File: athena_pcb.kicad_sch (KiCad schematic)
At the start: 36 parts, among them J2 Conn_01x04, SW1 SW_Push, U1 NRF5340-QKAA-R7, U2 BME280, Y1 32MHz, Y2 32.768kHz

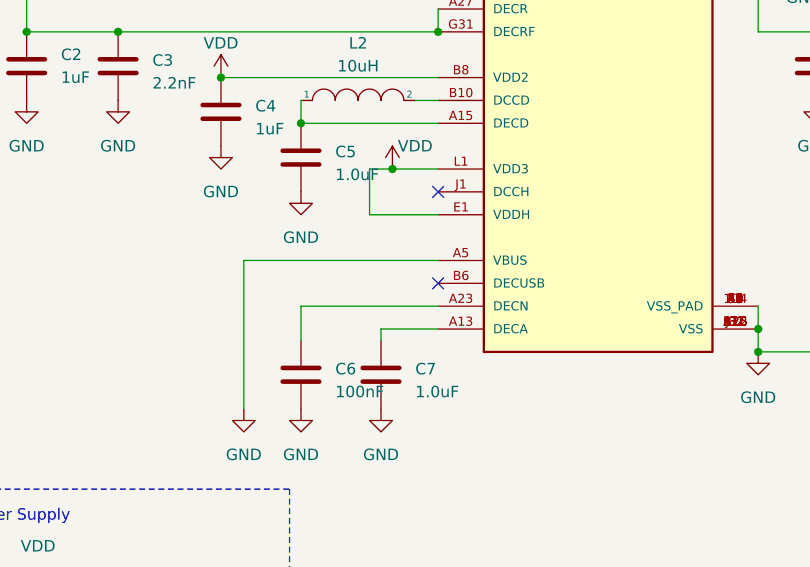
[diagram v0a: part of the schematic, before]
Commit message: Added items in the BOM
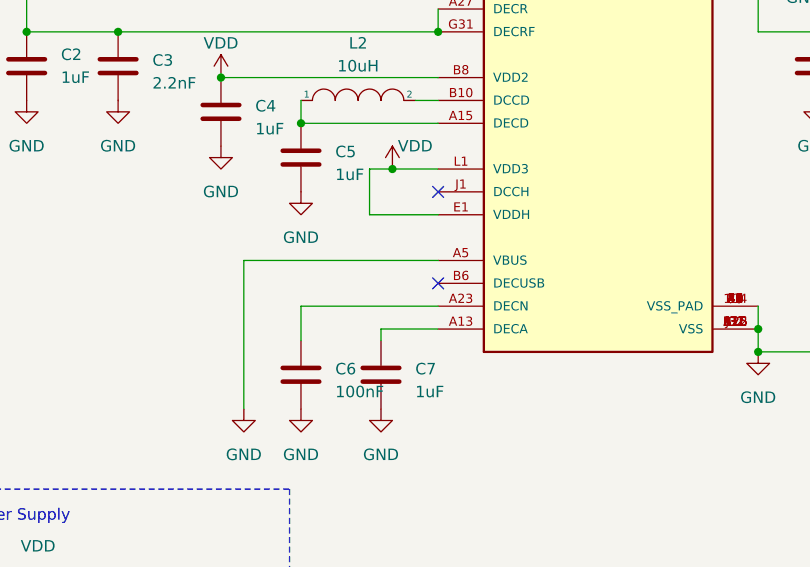
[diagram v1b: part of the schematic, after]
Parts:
- C1, C2, C4: MANUFACTURER (none) -> Murata; MPN (none) -> GRM155R61E105KA12D; Package (none) -> 0402
- C10, C11, C13, C14, C15, C16, C18, C19, C6, C8, C9: MANUFACTURER (none) -> Murata; MPN (none) -> GRM033R60J104KE19D; Package (none) -> 0201
- C12: MANUFACTURER (none) -> Murata; MPN (none) -> GJM0335C1HR70WB01D; Package (none) -> 0201
- C17: MANUFACTURER (none) -> N.A; MPN (none) -> N.A; Package (none) -> 0201
- C3: MANUFACTURER (none) -> Murata; MPN (none) -> GRM033R61A222KA01D; Package (none) -> 0201
- C5, C7: value 1.0uF -> 1uF; MANUFACTURER (none) -> Murata; MPN (none) -> GRM155R61E105KA12D; Package (none) -> 0402
- D1: Package (none) -> 0402
- L1, L2: Package (none) -> 0603
- L3, R1: Package (none) -> 0201
- U1: Package (none) -> AQFN-98
- U2: MANUFACTURER (none) -> Bosch; Package (none) -> LGA-8
- Y1: Package (none) -> XTAL_2016
- Y2: Package (none) -> XTAL_2012

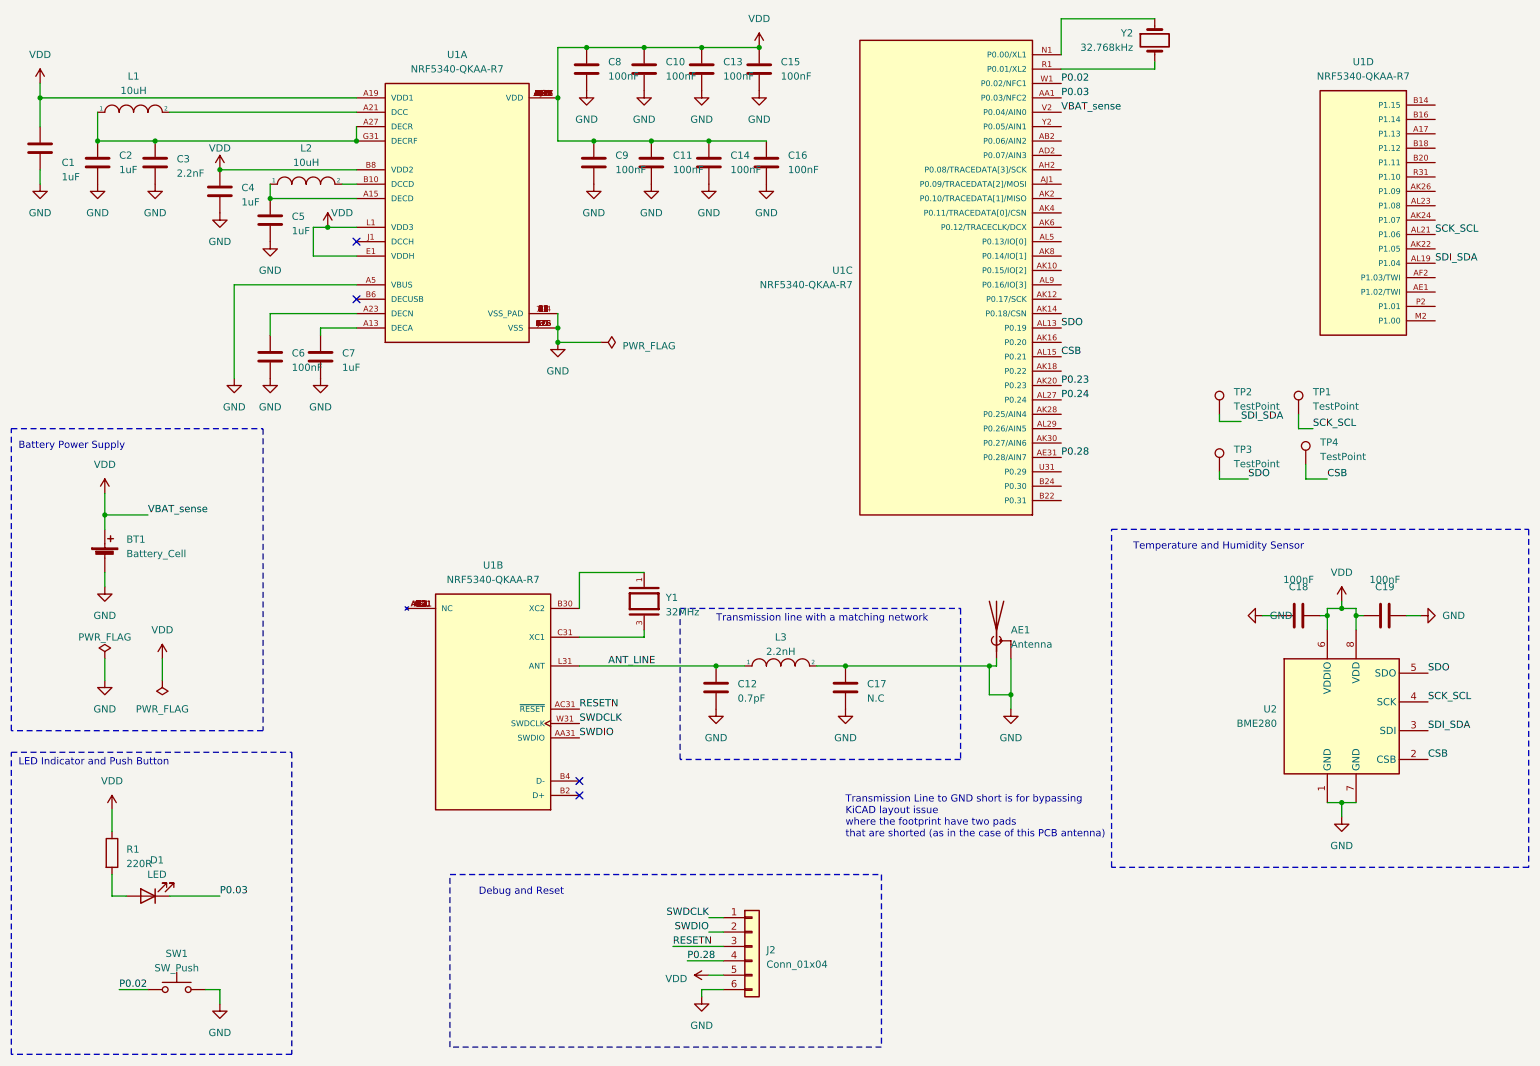
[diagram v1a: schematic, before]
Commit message: Bom updated, not connected added to nrf53 pins
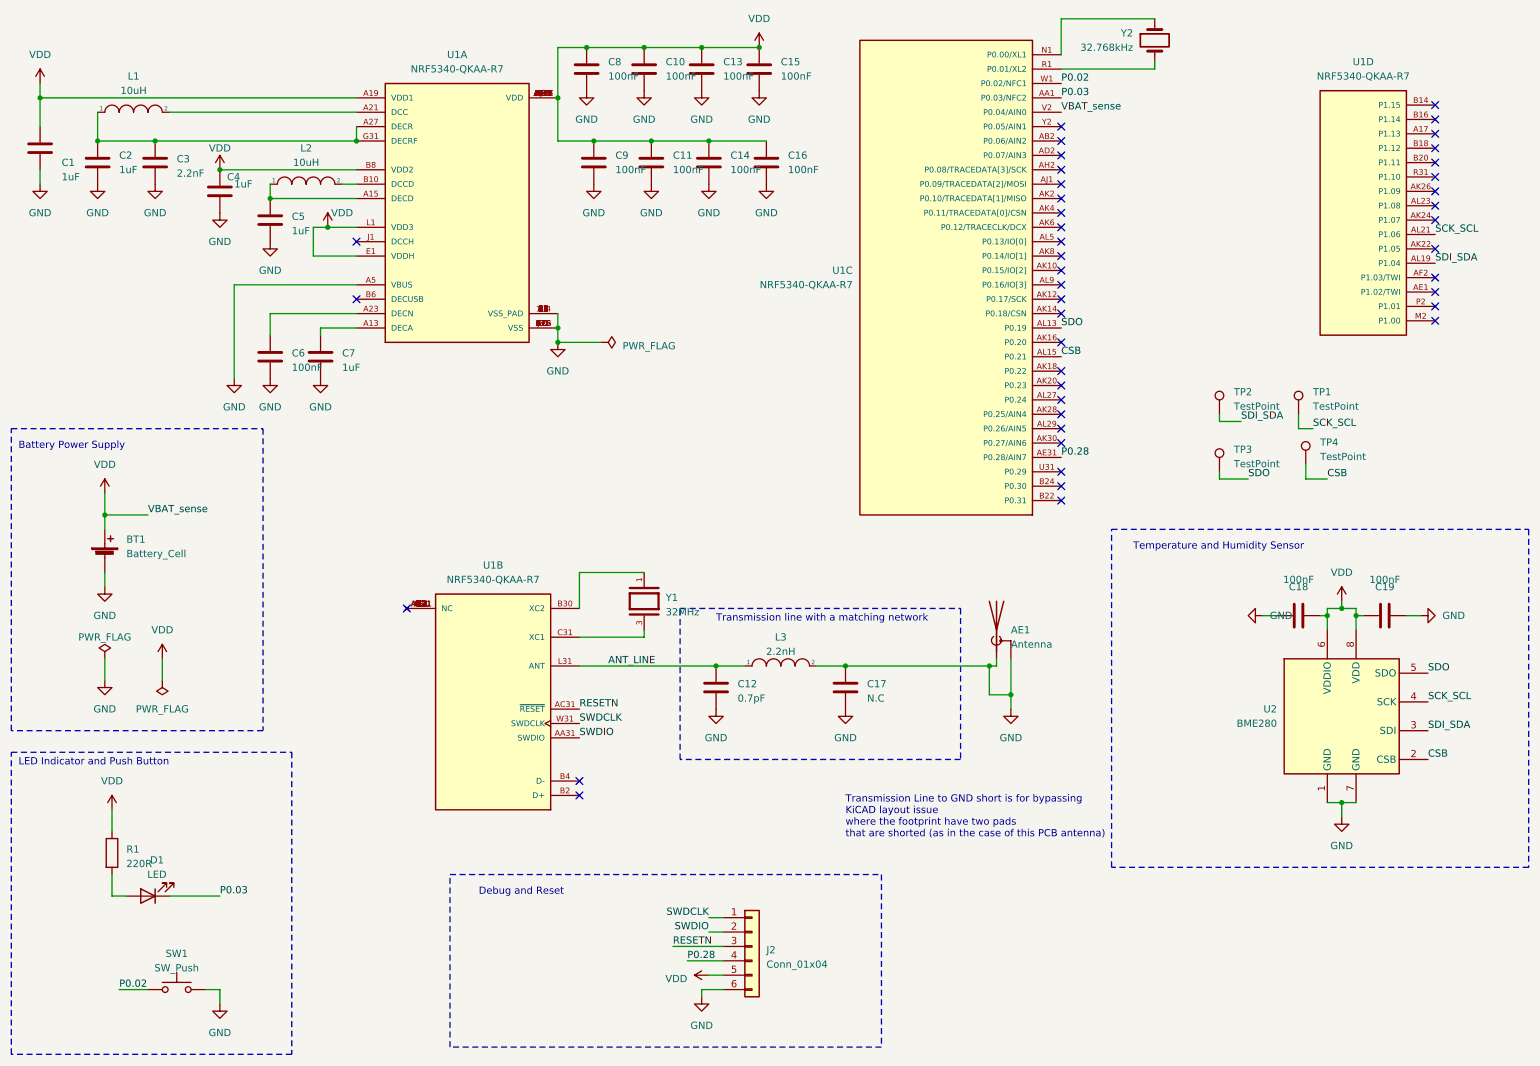
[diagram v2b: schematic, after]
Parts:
- AE1, J2: MANUFACTURER (none) -> N.A; MPN (none) -> N.A
- BT1: MANUFACTURER (none) -> Keystone; MPN (none) -> 1060
- L1, L2: MANUFACTURER (none) -> Murata; MPN (none) -> LQM18DN100M70L
- L3: MANUFACTURER (none) -> Murata; MPN (none) -> LQP03HQ2N2B02D
- R1: MANUFACTURER (none) -> YAGEO; MPN (none) -> RC0201FR-7D220RL
- SW1: MANUFACTURER (none) -> C&K Switches; MPN (none) -> KMR221NGLFS
- U1: MPN (none) -> nRF5340-QKAA-R7; Package AQFN-98 -> aQFN-94
- U2: MANUFACTURER Bosch -> Bosch Sensortec; MPN (none) -> BME280
- Y1: MPN (none) -> XRCGB32M000F1S1JR0
- Y2: MANUFACTURER (none) -> Micro Crystal; MPN (none) -> CM8V-T1A-32.768kHz-9pF-20PPM-TA-QC
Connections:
- net P0.23: no longer names the net of U1.AK20 (P0.23)
- net P0.24: no longer names the net of U1.AL27 (P0.24)
- no-connect marks 4 -> 43

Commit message: Added edge clearence, transmission line width to match with pcb antenna feed
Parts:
- D1: footprint LED_SMD:LED_0402_1005Metric -> LED_SMD:LED_0603_1608Metric; MANUFACTURER (none) -> Wurth Electronic; MPN (none) -> 150060VS55040; Package 0402 -> 0603
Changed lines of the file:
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@@
       (effects (font (size 1.27 1.27)))
     )
-    (property "Footprint" "LED_SMD:LED_0402_1005Metric" (at 39.37 168.91 0)
+    (property "Footprint" "LED_SMD:LED_0603_1608Metric" (at 39.37 168.91 0)
       (effects (font (size 1.27 1.27)) hide)
     )
@@
       (effects (font (size 1.27 1.27)) hide)
     )
-    (property "Package" "0402" (at 39.37 168.91 0)
+    (property "Package" "0603" (at 39.37 168.91 0)
       (effects (font (size 1.27 1.27)) hide)
     )
-    (property "MPN" "" (at 39.37 168.91 0)
+    (property "MPN" "150060VS55040" (at 39.37 168.91 0)
       (effects (font (size 1.27 1.27)) hide)
     )
-    (property "Description" "Green LED SMD" (at 39.37 168.91 0)
+    (property "Description" "Green LED SMD WL-SMCD " (at 39.37 168.91 0)
       (effects (font (size 1.27 1.27)) hide)
     )
+    (property "MANUFACTURER" "Wurth Electronic" (at 39.37 168.91 0)
+      (effects (font (size 1.27 1.27)) hide)
+    )

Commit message: Version sent to PCB manufacturer
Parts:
- AE1: Package (none) -> N.A
- C17: now not fitted
- J2: Package (none) -> N.A; now not fitted
- L1, L2: footprint Inductor_SMD:L_0603_1608Metric -> LQM18DN100M70L:INDC1608X95N
- L3: footprint Inductor_SMD:L_0201_0603Metric -> LQP03HQ2N2B02D:IND_LQP03HQ2N2B02D
- R1: value 220R -> 200R; footprint Resistor_SMD:R_0201_0603Metric -> Resistor_SMD:R_0402_1005Metric; MPN RC0201FR-7D220RL -> RC0402FR-13200RL; Package 0201 -> 0402
- TP1, TP2, TP3, TP4: MANUFACTURER (none) -> N.A; MPN (none) -> N.A; Package (none) -> N.A
- Y2: footprint Crystal:Crystal_SMD_2012-2Pin_2.0x1.2mm -> CM8V-T1A-32.768KHZ-9PF-20PPM-TA-QC:XTAL_CM8V-T1A-32.768KHZ-9PF-20PPM-TA-QC
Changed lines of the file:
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@@
       (effects (font (size 1.27 1.27)))
     )
-    (property "Footprint" "Inductor_SMD:L_0603_1608Metric" (at 67.31 43.18 0)
+    (property "Footprint" "LQM18DN100M70L:INDC1608X95N" (at 67.31 43.18 0)
       (effects (font (size 1.27 1.27)) hide)
     )
@@
   )
   (symbol (lib_id "Connector_Generic:Conn_01x06") (at 146.05 177.8 0) (unit 1)
-    (in_bom yes) (on_board yes) (dnp no) (fields_autoplaced)
+    (in_bom yes) (on_board yes) (dnp yes) (fields_autoplaced)
     (property "Reference" "J2" (at 148.59 178.435 0)
       (effects (font (size 1.27 1.27)) (justify left))
@@
       (effects (font (size 1.27 1.27)) hide)
     )
-    (property "Package" "" (at 146.05 177.8 0)
+    (property "Package" "N.A" (at 146.05 177.8 0)
       (effects (font (size 1.27 1.27)) hide)
     )
@@
       (effects (font (size 1.27 1.27)) hide)
     )
-    (property "Description" "Not mounted" (at 146.05 177.8 0)
+    (property "Description" "Not mounted/DNP" (at 146.05 177.8 0)
       (effects (font (size 1.27 1.27)) hide)
     )
@@
       (effects (font (size 1.27 1.27)) hide)
     )
-    (property "Package" "" (at 242.57 83.82 0)
-      (effects (font (size 1.27 1.27)) hide)
-    )
-    (property "MPN" "" (at 242.57 83.82 0)
+    (property "Package" "N.A" (at 242.57 83.82 0)
+      (effects (font (size 1.27 1.27)) hide)
+    )
+    (property "MPN" "N.A" (at 242.57 83.82 0)
       (effects (font (size 1.27 1.27)) hide)
     )
@@
       (effects (font (size 1.27 1.27)) hide)
     )
+    (property "MANUFACTURER" "N.A" (at 242.57 83.82 0)
+      (effects (font (size 1.27 1.27)) hide)
+    )
     (pin "1")
     (instances
@@
       (effects (font (size 1.27 1.27)) hide)
     )
-    (property "Package" "" (at 228.6 83.82 0)
-      (effects (font (size 1.27 1.27)) hide)
-    )
-    (property "MPN" "" (at 228.6 83.82 0)
+    (property "Package" "N.A" (at 228.6 83.82 0)
+      (effects (font (size 1.27 1.27)) hide)
+    )
+    (property "MPN" "N.A" (at 228.6 83.82 0)
       (effects (font (size 1.27 1.27)) hide)
     )
     (property "Description" "Test point pad" (at 228.6 83.82 0)
+      (effects (font (size 1.27 1.27)) hide)
+    )
+    (property "MANUFACTURER" "N.A" (at 228.6 83.82 0)
       (effects (font (size 1.27 1.27)) hide)
     )
@@
       (effects (font (size 1.27 1.27)) hide)
     )
-    (property "Package" "" (at 189.23 121.92 0)
+    (property "Package" "N.A" (at 189.23 121.92 0)
       (effects (font (size 1.27 1.27)) hide)
     )
@@
       (effects (font (size 1.27 1.27)) hide)
     )
-    (property "Package" "" (at 243.84 92.71 0)
-      (effects (font (size 1.27 1.27)) hide)
-    )
-    (property "MPN" "" (at 243.84 92.71 0)
+    (property "Package" "N.A" (at 243.84 92.71 0)
+      (effects (font (size 1.27 1.27)) hide)
+    )
+    (property "MPN" "N.A" (at 243.84 92.71 0)
       (effects (font (size 1.27 1.27)) hide)
     )
     (property "Description" "Test point pad" (at 243.84 92.71 0)
+      (effects (font (size 1.27 1.27)) hide)
+    )
+    (property "MANUFACTURER" "N.A" (at 243.84 92.71 0)
       (effects (font (size 1.27 1.27)) hide)
     )
@@
       (effects (font (size 1.27 1.27)))
     )
-    (property "Footprint" "Inductor_SMD:L_0201_0603Metric" (at 151.13 128.27 0)
+    (property "Footprint" "LQP03HQ2N2B02D:IND_LQP03HQ2N2B02D" (at 151.13 128.27 0)
       (effects (font (size 1.27 1.27)) hide)
     )
@@
       (effects (font (size 1.27 1.27)) hide)
     )
-    (property "Package" "" (at 228.6 93.98 0)
-      (effects (font (size 1.27 1.27)) hide)
-    )
-    (property "MPN" "" (at 228.6 93.98 0)
+    (property "Package" "N.A" (at 228.6 93.98 0)
+      (effects (font (size 1.27 1.27)) hide)
+    )
+    (property "MPN" "N.A" (at 228.6 93.98 0)
       (effects (font (size 1.27 1.27)) hide)
     )
     (property "Description" "Test point pad" (at 228.6 93.98 0)
+      (effects (font (size 1.27 1.27)) hide)
+    )
+    (property "MANUFACTURER" "N.A" (at 228.6 93.98 0)
       (effects (font (size 1.27 1.27)) hide)
     )
@@
       (effects (font (size 1.27 1.27)) (justify left))
     )
-    (property "Footprint" "Crystal:Crystal_SMD_2012-2Pin_2.0x1.2mm" (at 217.17 17.78 0)
+    (property "Footprint" "CM8V-T1A-32.768KHZ-9PF-20PPM-TA-QC:XTAL_CM8V-T1A-32.768KHZ-9PF-20PPM-TA-QC" (at 217.17 17.78 0)
       (effects (font (size 1.27 1.27)) hide)
     )
@@
       (effects (font (size 1.27 1.27)))
     )
-    (property "Footprint" "Inductor_SMD:L_0603_1608Metric" (at 36.83 30.48 0)
+    (property "Footprint" "LQM18DN100M70L:INDC1608X95N" (at 36.83 30.48 0)
       (effects (font (size 1.27 1.27)) hide)
     )
@@
   )
   (symbol (lib_id "Device:C") (at 162.56 132.08 0) (unit 1)
-    (in_bom yes) (on_board yes) (dnp no) (fields_autoplaced)
+    (in_bom yes) (on_board yes) (dnp yes) (fields_autoplaced)
     (property "Reference" "C17" (at 166.37 131.445 0)
       (effects (font (size 1.27 1.27)) (justify left))
@@
       (effects (font (size 1.27 1.27)) hide)
     )
-    (property "Description" "Not mounted" (at 162.56 132.08 0)
+    (property "Description" "Not mounted/DNP" (at 162.56 132.08 0)
       (effects (font (size 1.27 1.27)) hide)
     )
@@
       (effects (font (size 1.27 1.27)) (justify left))
     )
-    (property "Value" "220R" (at 35.56 163.195 0)
-      (effects (font (size 1.27 1.27)) (justify left))
-    )
-    (property "Footprint" "Resistor_SMD:R_0201_0603Metric" (at 31.242 161.29 90)
+    (property "Value" "200R" (at 35.56 163.195 0)
+      (effects (font (size 1.27 1.27)) (justify left))
+    )
+    (property "Footprint" "Resistor_SMD:R_0402_1005Metric" (at 31.242 161.29 90)
       (effects (font (size 1.27 1.27)) hide)
     )
@@
       (effects (font (size 1.27 1.27)) hide)
     )
-    (property "Package" "0201" (at 33.02 161.29 0)
-      (effects (font (size 1.27 1.27)) hide)
-    )
-    (property "MPN" "RC0201FR-7D220RL" (at 33.02 161.29 0)
-      (effects (font (size 1.27 1.27)) hide)
-    )
-    (property "Description" "Resistor, ±1%, 0.05W" (at 33.02 161.29 0)
-      (effects (font (size 1.27 1.27)) hide)
-    )
+    (property "Package" "0402" (at 33.02 161.29 0)
+      (effects (font (size 1.27 1.27)) hide)
+    )
+    (property "MPN" "RC0402FR-13200RL" (at 33.02 161.29 0)
+      (effects (font (size 1.27 1.27)) hide)
+    )
+    (property "Description" "Resistor, ±1%, 62.5 mW" (at 33.02 161.29 0)
+      (effects (font (size 1.27 1.27)) hide)
+    )
